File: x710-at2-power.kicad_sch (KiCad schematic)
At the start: 121 parts, among them U4 EZX710AT2_S_LMR5

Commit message: [#80813] Add OCuLink connector
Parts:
- renumbered C35 to C100, C36 to C101, C37 to C102, C38 to C103, C81 to C104, C82 to C105, C83 to C106, C84 to C107, C85 to C108, C86 to C109, C108 to C110, C13 to C111, C12 to C112, C11 to C113, C10 to C114, C109 to C115, C110 to C116, C118 to C117, C119 to C118, C117 to C119, C113 to C120, C114 to C121, C115 to C122, C116 to C123, C111 to C124, C112 to C125, C125 to C126, C126 to C127, C124 to C128, C120 to C129, C121 to C130, C122 to C131, C123 to C132, C135 to C133, C140 to C134, C136 to C135, C137 to C136, C138 to C137, C139 to C138, C141 to C139, C143 to C140, C142 to C141, C144 to C142, C145 to C143, C87 to C32, C88 to C33, C89 to C34, C90 to C35, C91 to C36, C92 to C37, C93 to C38, C94 to C39, C95 to C40, C74 to C41, C63 to C42, C64 to C43, C65 to C44, C66 to C45, C67 to C46, C68 to C47, C69 to C48, C70 to C49, C71 to C50, C72 to C51, C73 to C52, C146 to C53, C147 to C54, C148 to C55, C149 to C56, C150 to C57, C151 to C58, C40 to C59, C41 to C60, C42 to C61, C43 to C62, C44 to C63, C45 to C64, C46 to C65, C47 to C66, C48 to C67, C49 to C68, C50 to C69, C51 to C70, C52 to C71, C53 to C72, C54 to C73, C55 to C74, C56 to C75, C61 to C76, C62 to C77, C59 to C78, C60 to C79, C58 to C80, C57 to C81, C152 to C82, C153 to C83, C34 to C84, C75 to C85, C76 to C86, C77 to C87, C78 to C88, C79 to C89, C80 to C90, C39 to C91, C127 to C92, C132 to C93, C133 to C94, C128 to C95, C129 to C96, C130 to C97, C131 to C98, C134 to C99, FB7 to FB3, FB5 to FB4, FB2 to FB5, FB4 to FB6, FB6 to FB7, L6 to L3

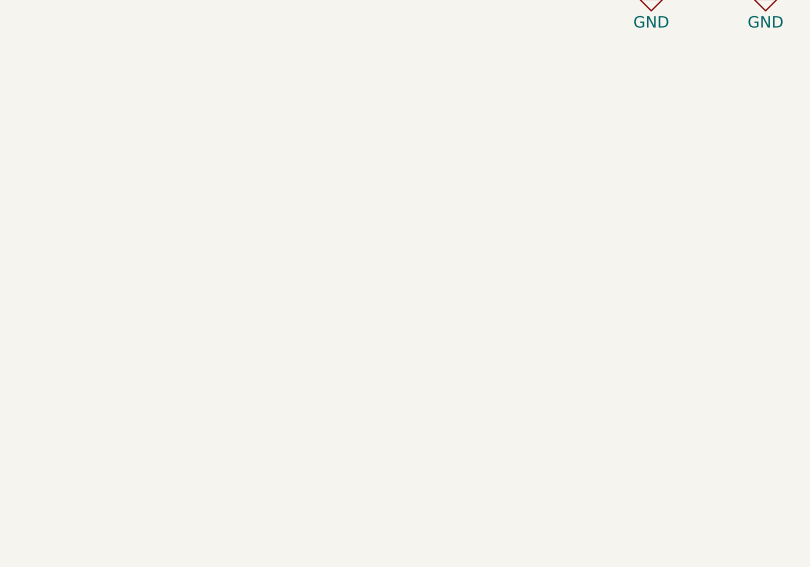
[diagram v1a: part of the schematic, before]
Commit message: [#80813] Add power input connectors, heatsink, mounting, draft component placement
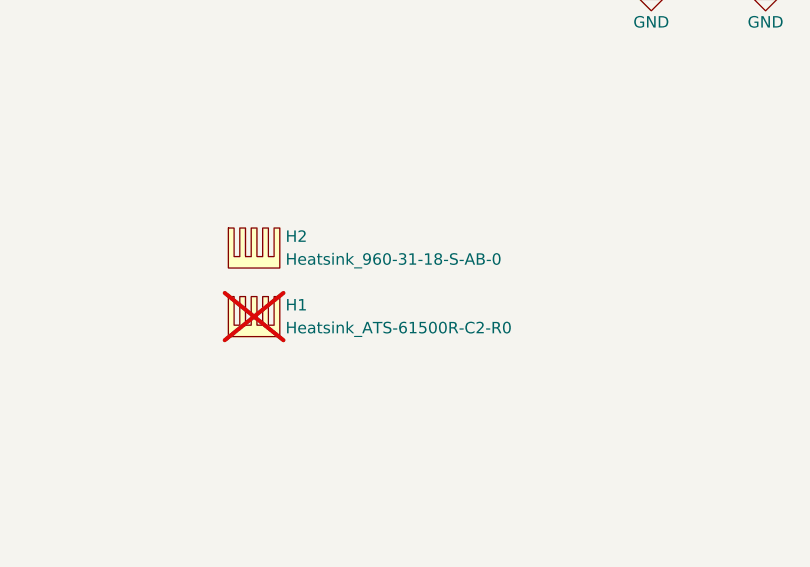
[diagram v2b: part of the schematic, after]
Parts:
- added H1: Heatsink_ATS-61500R-C2-R0, antmicro-footprints:Heatsink_ATS-61500R-C2-R0, symbol antmicroMechanicalParts:Heatsink_ATS-61500R-C2-R0
- added H2: Heatsink_960-31-18-S-AB-0, antmicro-footprints:Heatsink_960-31-18-S-AB-0, symbol antmicroMechanicalParts:Heatsink_960-31-18-S-AB-0
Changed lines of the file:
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@@
 	)
 	(symbol
+		(lib_id "antmicroMechanicalParts:Heatsink_960-31-18-S-AB-0")
+		(at 223.52 179.07 0)
+		(unit 1)
+		(exclude_from_sim no)
+		(in_bom yes)
+		(on_board yes)
+		(dnp no)
+		(fields_autoplaced yes)
+		(property "Reference" "H2"
+			(at 229.87 180.0225 0)
+			(effects
+				(font
+					(size 1.27 1.27)
+					(thickness 0.15)
+				)
+				(justify left)
+			)
+		)
+		(property "Value" "Heatsink_960-31-18-S-AB-0"
+			(at 229.87 182.5625 0)
+			(effects
+				(font
+					(size 1.27 1.27)
+					(thickness 0.15)
+				)
+				(justify left)
+			)
+		)
+		(property "Footprint" "antmicro-footprints:Heatsink_960-31-18-S-AB-0"
+			(at 241.3 186.69 0)
+			(effects
+				(font
+					(size 1.27 1.27)
+					(thickness 0.15)
+				)
+				(justify left bottom)
+				(hide yes)
+			)
+		)
+		(property "Datasheet" "https://media.digikey.com/pdf/Data%20Sheets/Wakefield%20Thermal%20PDFs/960_Series.pdf"
+			(at 241.3 189.23 0)
+			(effects
+				(font
+					(size 1.27 1.27)
+					(thickness 0.15)
+				)
+				(justify left bottom)
+				(hide yes)
+			)
+		)
+		(property "Description" "Heat Sink BGA Aluminum Top Mount"
+			(at 223.52 179.07 0)
+			(effects
+				(font
+					(size 1.27 1.27)
+				)
+				(hide yes)
+			)
+		)
+		(property "MPN" "960-31-18-S-AB-0"
+			(at 241.3 191.77 0)
+			(effects
+				(font
+					(size 1.27 1.27)
+					(thickness 0.15)
+				)
+				(justify left bottom)
+				(hide yes)
+			)
+		)
+		(property "Manufacturer" "Wakefield-Vette"
+			(at 241.3 194.31 0)
+			(effects
+				(font
+					(size 1.27 1.27)
+					(thickness 0.15)
+				)
+				(justify left bottom)
+				(hide yes)
+			)
+		)
+		(property "Author" "Antmicro"
+			(at 241.3 196.85 0)
+			(effects
+				(font
+					(size 1.27 1.27)
+					(thickness 0.15)
+				)
+				(justify left bottom)
+				(hide yes)
+			)
+		)
+		(property "License" "Apache-2.0"
+			(at 241.3 199.39 0)
+			(effects
+				(font
+					(size 1.27 1.27)
+					(thickness 0.15)
+				)
+				(justify left bottom)
+				(hide yes)
+			)
+		)
+		(instances
+			(project ""
+				(path "/04bda987-e5eb-48b4-9e90-d8211dc11b39/745fdd8b-25af-4553-a7ea-a0fa564ee0a7"
+					(reference "H2")
+					(unit 1)
+				)
+			)
+		)
+	)
+	(symbol
 		(lib_id "antmicropower:GND")
 		(at 361.95 76.2 0)
@@
 					(unit 1)
 				)
+			)
+		)
+	)
+	(symbol
+		(lib_id "antmicroMechanicalParts:Heatsink_ATS-61500R-C2-R0")
+		(at 223.52 186.69 0)
+		(unit 1)
+		(exclude_from_sim no)
+		(in_bom no)
+		(on_board yes)
+		(dnp yes)
+		(fields_autoplaced yes)
+		(property "Reference" "H1"
+			(at 229.87 187.6425 0)
+			(effects
+				(font
+					(size 1.27 1.27)
+					(thickness 0.15)
+				)
+				(justify left)
+			)
+		)
+		(property "Value" "Heatsink_ATS-61500R-C2-R0"
+			(at 229.87 190.1825 0)
+			(effects
+				(font
+					(size 1.27 1.27)
+					(thickness 0.15)
+				)
+				(justify left)
+			)
+		)
+		(property "Footprint" "antmicro-footprints:Heatsink_ATS-61500R-C2-R0"
+			(at 241.3 194.31 0)
+			(effects
+				(font
+					(size 1.27 1.27)
+					(thickness 0.15)
+				)
+				(justify left bottom)
+				(hide yes)
+			)
+		)
+		(property "Datasheet" "https://www.qats.com/DataSheet/ATS-61500-Series-C2-R0"
+			(at 241.3 196.85 0)
+			(effects
+				(font
+					(size 1.27 1.27)
+					(thickness 0.15)
+				)
+				(justify left bottom)
+				(hide yes)
+			)
+		)
+		(property "Description" "Heat Sinks fanSINK Assembly with Mounting Hardware"
+			(at 223.52 186.69 0)
+			(effects
+				(font
+					(size 1.27 1.27)
+				)
+				(hide yes)
+			)
+		)
+		(property "MPN" "ATS-61500R-C2-R0"
+			(at 241.3 199.39 0)
+			(effects
+				(font
+					(size 1.27 1.27)
+					(thickness 0.15)
+				)
+				(justify left bottom)
+				(hide yes)
+			)
+		)
+		(property "Manufacturer" "Advanced Thermal Solutions"
+			(at 241.3 201.93 0)
+			(effects
+				(font
+					(size 1.27 1.27)
+					(thickness 0.15)
+				)
+				(justify left bottom)
+				(hide yes)
+			)
+		)
+		(property "Author" "Antmicro"
+			(at 241.3 204.47 0)
+			(effects
+				(font
+					(size 1.27 1.27)
+					(thickness 0.15)
+				)
+				(justify left bottom)
+				(hide yes)
+			)
+		)
+		(property "License" "Apache-2.0"
+			(at 241.3 207.01 0)
+			(effects
+				(font
+					(size 1.27 1.27)
+					(thickness 0.15)
+				)
+				(justify left bottom)
+				(hide yes)
+			)
+		)
+		(instances
+			(project ""
+				(path "/04bda987-e5eb-48b4-9e90-d8211dc11b39/745fdd8b-25af-4553-a7ea-a0fa564ee0a7"
+					(reference "H1")
+					(unit 1)
+				)

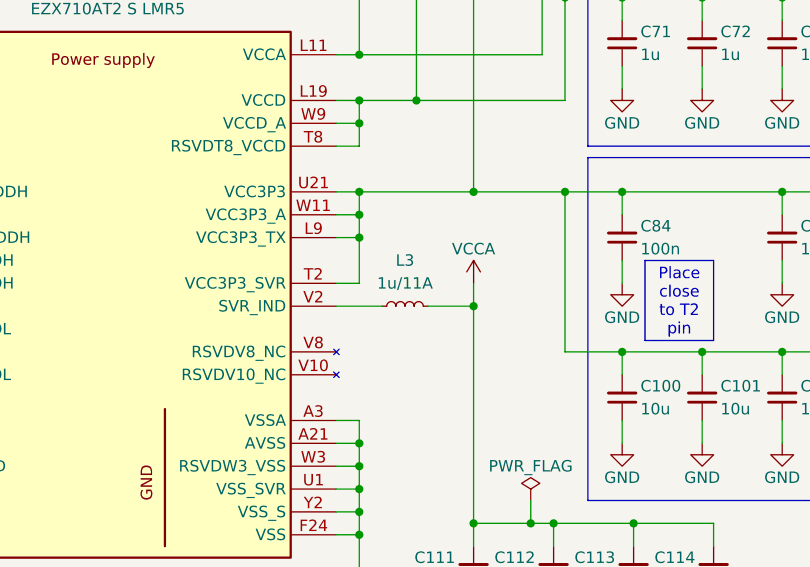
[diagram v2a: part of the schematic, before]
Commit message: [#80813] Change inductors, minor PCB changes
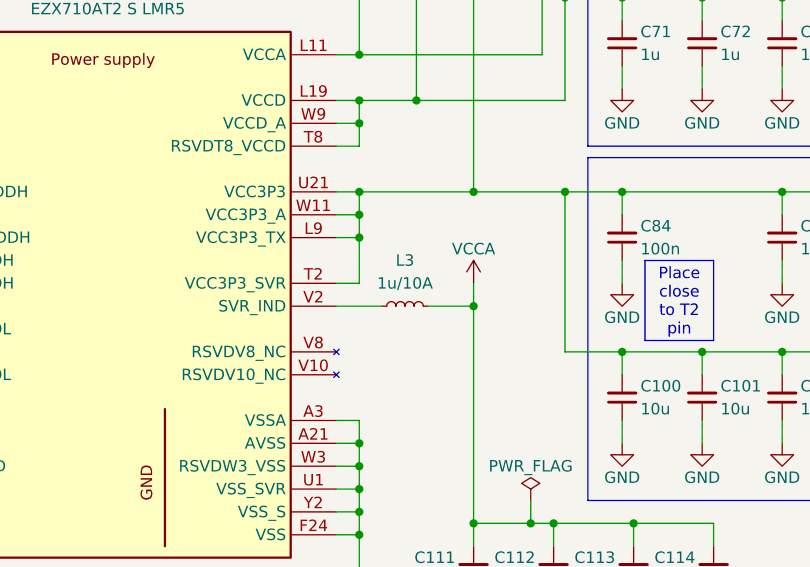
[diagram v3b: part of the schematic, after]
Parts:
- removed L3: L_1u_11A_Coilcraft-XFL4020, antmicro-footprints:L_Coilcraft-XFL4020, symbol antmicroFixedInductors:L_1u_11A_Coilcraft-XFL4020
- added L3: L_1u_10A_Bourns-SRP4021HMT, antmicro-footprints:L_Bourns-SRP4021HMT, symbol antmicroFixedInductors:L_1u_10A_Bourns-SRP4021HMT
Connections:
- net VCCA: now also L3.2
- net at U4.V2 (SVR_IND): now also L3.1
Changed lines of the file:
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@@
 	)
 	(symbol
+		(lib_id "antmicroFixedInductors:L_1u_10A_Bourns-SRP4021HMT")
+		(at 273.05 118.11 0)
+		(unit 1)
+		(exclude_from_sim no)
+		(in_bom yes)
+		(on_board yes)
+		(dnp no)
+		(fields_autoplaced yes)
+		(property "Reference" "L3"
+			(at 275.59 113.03 0)
+			(effects
+				(font
+					(size 1.27 1.27)
+					(thickness 0.15)
+				)
+			)
+		)
+		(property "Value" "L_1u_10A_Bourns-SRP4021HMT"
+			(at 288.29 128.27 0)
+			(effects
+				(font
+					(size 1.27 1.27)
+					(thickness 0.15)
+				)
+				(justify left bottom)
+				(hide yes)
+			)
+		)
+		(property "Footprint" "antmicro-footprints:L_Bourns-SRP4021HMT"
+			(at 288.29 130.81 0)
+			(effects
+				(font
+					(size 1.27 1.27)
+					(thickness 0.15)
+				)
+				(justify left bottom)
+				(hide yes)
+			)
+		)
+		(property "Datasheet" "https://www.mouser.pl/datasheet/2/54/Bourns_04_01_2025_SRP4021HMT_Datasheet-3580094.pdf"
+			(at 288.29 133.35 0)
+			(effects
+				(font
+					(size 1.27 1.27)
+					(thickness 0.15)
+				)
+				(justify left bottom)
+				(hide yes)
+			)
+		)
+		(property "Description" "Power Inductors - SMD Ind,4.1x4.2x1.9mm,1uH+/-20%,10A, Shielded"
+			(at 288.29 135.89 0)
+			(effects
+				(font
+					(size 1.27 1.27)
+					(thickness 0.15)
+				)
+				(justify left bottom)
+				(hide yes)
+			)
+		)
+		(property "Val" "1u/10A"
+			(at 275.59 115.57 0)
+			(effects
+				(font
+					(size 1.27 1.27)
+					(thickness 0.15)
+				)
+			)
+		)
+		(property "Manufacturer" "Bourns"
+			(at 288.29 138.43 0)
+			(effects
+				(font
+					(size 1.27 1.27)
+					(thickness 0.15)
+				)
+				(justify left bottom)
+				(hide yes)
+			)
+		)
+		(property "MPN" "SRP4021HMT-1R0M"
+			(at 288.29 140.97 0)
+			(effects
+				(font
+					(size 1.27 1.27)
+					(thickness 0.15)
+				)
+				(justify left bottom)
+				(hide yes)
+			)
+		)
+		(property "ISat" ""
+			(at 287.02 134.62 0)
+			(effects
+				(font
+					(size 1.27 1.27)
+				)
+				(justify left)
+				(hide yes)
+			)
+		)
+		(property "Isat" "8A"
+			(at 288.29 143.51 0)
+			(effects
+				(font
+					(size 1.27 1.27)
+					(thickness 0.15)
+				)
+				(justify left bottom)
+				(hide yes)
+			)
+		)
+		(property "IMax" ""
+			(at 287.02 138.43 0)
+			(effects
+				(font
+					(size 1.27 1.27)
+					(thickness 0.15)
+				)
+				(justify left bottom)
+				(hide yes)
+			)
+		)
+		(property "Imax" "10A"
+			(at 288.29 146.05 0)
+			(effects
+				(font
+					(size 1.27 1.27)
+					(thickness 0.15)
+				)
+				(justify left bottom)
+				(hide yes)
+			)
+		)
+		(property "Size" "4.2x4.1"
+			(at 288.29 148.59 0)
+			(effects
+				(font
+					(size 1.27 1.27)
+					(thickness 0.15)
+				)
+				(justify left bottom)
+				(hide yes)
+			)
+		)
+		(property "Author" "Antmicro"
+			(at 288.29 151.13 0)
+			(effects
+				(font
+					(size 1.27 1.27)
+					(thickness 0.15)
+				)
+				(justify left bottom)
+				(hide yes)
+			)
+		)
+		(property "License" "Apache-2.0"
+			(at 288.29 153.67 0)
+			(effects
+				(font
+					(size 1.27 1.27)
+					(thickness 0.15)
+				)
+				(justify left bottom)
+				(hide yes)
+			)
+		)
+		(pin "1"
+		)
+		(pin "2"
+		)
+		(instances
+			(project "10-gbe-expansion"
+				(path "/04bda987-e5eb-48b4-9e90-d8211dc11b39/745fdd8b-25af-4553-a7ea-a0fa564ee0a7"
+					(reference "L3")
+					(unit 1)
+				)
+			)
+		)
+	)
+	(symbol
 		(lib_id "antmicroFerriteBeadsandChips:FB_33Z_3A_Murata-BLM18PG_0603")
 		(at 45.72 172.72 0)
@@
 					(unit 1)
 				)
-			)
-		)
-	)
-	(symbol
-		(lib_id "antmicroFixedInductors:L_1u_11A_Coilcraft-XFL4020")
-		(at 273.05 118.11 0)
-		(unit 1)
-		(exclude_from_sim no)
-		(in_bom yes)
-		(on_board yes)
-		(dnp no)
-		(fields_autoplaced yes)
-		(property "Reference" "L3"
-			(at 275.59 113.03 0)
-			(effects
-				(font
-					(size 1.27 1.27)
-					(thickness 0.15)
-				)
-			)
-		)
-		(property "Value" "L_1u_11A_Coilcraft-XFL4020"
-			(at 287.02 120.65 0)
-			(effects
-				(font
-					(size 1.27 1.27)
-					(thickness 0.15)
-				)
-				(justify left bottom)
-				(hide yes)
-			)
-		)
-		(property "Footprint" "antmicro-footprints:L_Coilcraft-XFL4020"
-			(at 287.02 125.73 0)
-			(effects
-				(font
-					(size 1.27 1.27)
-					(thickness 0.15)
-				)
-				(justify left bottom)
-				(hide yes)
-			)
-		)
-		(property "Datasheet" "https://www.coilcraft.com/getmedia/50632d43-da1b-4cdb-8ab4-3029cab51df3/xfl4020.pdf"
-			(at 287.02 128.27 0)
-			(effects
-				(font
-					(size 1.27 1.27)
-					(thickness 0.15)
-				)
-				(justify left bottom)
-				(hide yes)
-			)
-		)
-		(property "Description" "Power Inductor (SMD), 1 µH, 11 A, Shielded, 4.5 A, XFL4020"
-			(at 273.05 118.11 0)
-			(effects
-				(font
-					(size 1.27 1.27)
-				)
-				(hide yes)
-			)
-		)
-		(property "Val" "1u/11A"
-			(at 275.59 115.57 0)
-			(effects
-				(font
-					(size 1.27 1.27)
-					(thickness 0.15)
-				)
-			)
-		)
-		(property "Manufacturer" "Coilcraft"
-			(at 287.02 130.81 0)
-			(effects
-				(font
-					(size 1.27 1.27)
-					(thickness 0.15)
-				)
-				(justify left bottom)
-				(hide yes)
-			)
-		)
-		(property "MPN" "XFL4020-102MEC"
-			(at 287.02 133.35 0)
-			(effects
-				(font
-					(size 1.27 1.27)
-					(thickness 0.15)
-				)
-				(justify left bottom)
-				(hide yes)
-			)
-		)
-		(property "ISat" "5.4 A"
-			(at 287.02 134.62 0)
-			(effects
-				(font
-					(size 1.27 1.27)
-				)
-				(justify left)
-				(hide yes)
-			)
-		)
-		(property "IMax" "11 A"
-			(at 287.02 138.43 0)
-			(effects
-				(font
-					(size 1.27 1.27)
-					(thickness 0.15)
-				)
-				(justify left bottom)
-				(hide yes)
-			)
-		)
-		(property "Size" "4.3x4.3"
-			(at 287.02 140.97 0)
-			(effects
-				(font
-					(size 1.27 1.27)
-					(thickness 0.15)
-				)
-				(justify left bottom)
-				(hide yes)
-			)
-		)
-		(property "Author" "Antmicro"
-			(at 287.02 143.51 0)
-			(effects
-				(font
-					(size 1.27 1.27)
-					(thickness 0.15)
-				)
-				(justify left bottom)
-				(hide yes)
-			)
-		)
-		(property "License" "Apache-2.0"
-			(at 287.02 146.05 0)
-			(effects
-				(font
-					(size 1.27 1.27)
-					(thickness 0.15)
-				)
-				(justify left bottom)
-				(hide yes)
-			)
-		)
-		(pin "1"
-		)
-		(pin "2"
-		)
-		(instances
-			(project ""
-				(path "/04bda987-e5eb-48b4-9e90-d8211dc11b39/745fdd8b-25af-4553-a7ea-a0fa564ee0a7"
-					(reference "L3")
-					(unit 1)
-				)

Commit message: [#81595] Update symbols from library
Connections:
- no-connect marks 0 -> 2
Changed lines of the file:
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@@
 		(color 0 0 0 0)
 	)
+	(no_connect
+		(at 267.97 125.73)
+	)
+	(no_connect
+		(at 267.97 123.19)
+	)
 	(wire
 		(pts
@@
 			)
 		)
-		(property "Datasheet" "https://www.mouser.pl/datasheet/2/54/Bourns_04_01_2025_SRP4021HMT_Datasheet-3580094.pdf"
+		(property "Datasheet" "https://www.mouser.com/datasheet/2/54/Bourns_04_01_2025_SRP4021HMT_Datasheet-3580094.pdf"
 			(at 288.29 133.35 0)
 			(effects
@@
 		(pin "M22"
 		)
-		(pin "M31"
+		(pin "V34"
 		)
 		(pin "G27"
@@
 		(pin "J39"
 		)
-		(pin "M15"
-		)
 		(pin "D42"

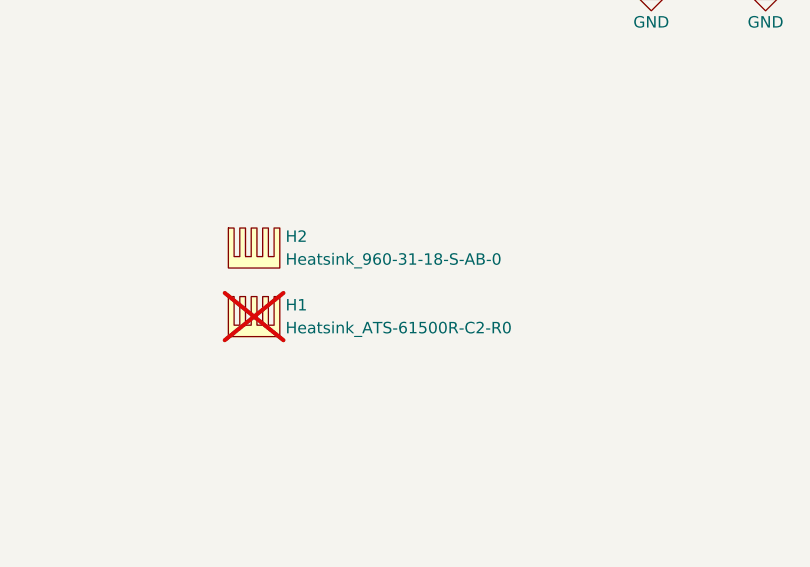
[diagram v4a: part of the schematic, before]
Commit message: [#85196] Update PCB from schematic, remove second heat sink
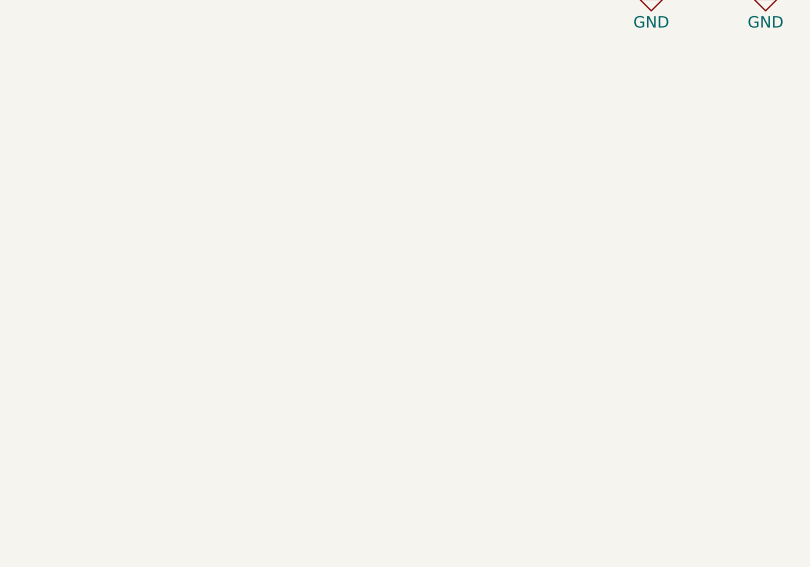
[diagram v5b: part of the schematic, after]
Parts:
- removed H1: Heatsink_ATS-61500R-C2-R0, antmicro-footprints:Heatsink_ATS-61500R-C2-R0, symbol antmicroMechanicalParts:Heatsink_ATS-61500R-C2-R0
- removed H2: Heatsink_960-31-18-S-AB-0, antmicro-footprints:Heatsink_960-31-18-S-AB-0, symbol antmicroMechanicalParts:Heatsink_960-31-18-S-AB-0
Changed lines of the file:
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@@
 	)
 	(symbol
-		(lib_id "antmicroMechanicalParts:Heatsink_960-31-18-S-AB-0")
-		(at 223.52 179.07 0)
-		(unit 1)
-		(exclude_from_sim no)
-		(in_bom yes)
-		(on_board yes)
-		(dnp no)
-		(fields_autoplaced yes)
-		(property "Reference" "H2"
-			(at 229.87 180.0225 0)
-			(effects
-				(font
-					(size 1.27 1.27)
-					(thickness 0.15)
-				)
-				(justify left)
-			)
-		)
-		(property "Value" "Heatsink_960-31-18-S-AB-0"
-			(at 229.87 182.5625 0)
-			(effects
-				(font
-					(size 1.27 1.27)
-					(thickness 0.15)
-				)
-				(justify left)
-			)
-		)
-		(property "Footprint" "antmicro-footprints:Heatsink_960-31-18-S-AB-0"
-			(at 241.3 186.69 0)
-			(effects
-				(font
-					(size 1.27 1.27)
-					(thickness 0.15)
-				)
-				(justify left bottom)
-				(hide yes)
-			)
-		)
-		(property "Datasheet" "https://media.digikey.com/pdf/Data%20Sheets/Wakefield%20Thermal%20PDFs/960_Series.pdf"
-			(at 241.3 189.23 0)
-			(effects
-				(font
-					(size 1.27 1.27)
-					(thickness 0.15)
-				)
-				(justify left bottom)
-				(hide yes)
-			)
-		)
-		(property "Description" "Heat Sink BGA Aluminum Top Mount"
-			(at 223.52 179.07 0)
-			(effects
-				(font
-					(size 1.27 1.27)
-				)
-				(hide yes)
-			)
-		)
-		(property "MPN" "960-31-18-S-AB-0"
-			(at 241.3 191.77 0)
-			(effects
-				(font
-					(size 1.27 1.27)
-					(thickness 0.15)
-				)
-				(justify left bottom)
-				(hide yes)
-			)
-		)
-		(property "Manufacturer" "Wakefield-Vette"
-			(at 241.3 194.31 0)
-			(effects
-				(font
-					(size 1.27 1.27)
-					(thickness 0.15)
-				)
-				(justify left bottom)
-				(hide yes)
-			)
-		)
-		(property "Author" "Antmicro"
-			(at 241.3 196.85 0)
-			(effects
-				(font
-					(size 1.27 1.27)
-					(thickness 0.15)
-				)
-				(justify left bottom)
-				(hide yes)
-			)
-		)
-		(property "License" "Apache-2.0"
-			(at 241.3 199.39 0)
-			(effects
-				(font
-					(size 1.27 1.27)
-					(thickness 0.15)
-				)
-				(justify left bottom)
-				(hide yes)
-			)
-		)
-		(instances
-			(project ""
-				(path "/04bda987-e5eb-48b4-9e90-d8211dc11b39/745fdd8b-25af-4553-a7ea-a0fa564ee0a7"
-					(reference "H2")
-					(unit 1)
-				)
-			)
-		)
-	)
-	(symbol
 		(lib_id "antmicropower:GND")
 		(at 361.95 76.2 0)
@@
 					(unit 1)
 				)
-			)
-		)
-	)
-	(symbol
-		(lib_id "antmicroMechanicalParts:Heatsink_ATS-61500R-C2-R0")
-		(at 223.52 186.69 0)
-		(unit 1)
-		(exclude_from_sim no)
-		(in_bom no)
-		(on_board yes)
-		(dnp yes)
-		(fields_autoplaced yes)
-		(property "Reference" "H1"
-			(at 229.87 187.6425 0)
-			(effects
-				(font
-					(size 1.27 1.27)
-					(thickness 0.15)
-				)
-				(justify left)
-			)
-		)
-		(property "Value" "Heatsink_ATS-61500R-C2-R0"
-			(at 229.87 190.1825 0)
-			(effects
-				(font
-					(size 1.27 1.27)
-					(thickness 0.15)
-				)
-				(justify left)
-			)
-		)
-		(property "Footprint" "antmicro-footprints:Heatsink_ATS-61500R-C2-R0"
-			(at 241.3 194.31 0)
-			(effects
-				(font
-					(size 1.27 1.27)
-					(thickness 0.15)
-				)
-				(justify left bottom)
-				(hide yes)
-			)
-		)
-		(property "Datasheet" "https://www.qats.com/DataSheet/ATS-61500-Series-C2-R0"
-			(at 241.3 196.85 0)
-			(effects
-				(font
-					(size 1.27 1.27)
-					(thickness 0.15)
-				)
-				(justify left bottom)
-				(hide yes)
-			)
-		)
-		(property "Description" "Heat Sinks fanSINK Assembly with Mounting Hardware"
-			(at 223.52 186.69 0)
-			(effects
-				(font
-					(size 1.27 1.27)
-				)
-				(hide yes)
-			)
-		)
-		(property "MPN" "ATS-61500R-C2-R0"
-			(at 241.3 199.39 0)
-			(effects
-				(font
-					(size 1.27 1.27)
-					(thickness 0.15)
-				)
-				(justify left bottom)
-				(hide yes)
-			)
-		)
-		(property "Manufacturer" "Advanced Thermal Solutions"
-			(at 241.3 201.93 0)
-			(effects
-				(font
-					(size 1.27 1.27)
-					(thickness 0.15)
-				)
-				(justify left bottom)
-				(hide yes)
-			)
-		)
-		(property "Author" "Antmicro"
-			(at 241.3 204.47 0)
-			(effects
-				(font
-					(size 1.27 1.27)
-					(thickness 0.15)
-				)
-				(justify left bottom)
-				(hide yes)
-			)
-		)
-		(property "License" "Apache-2.0"
-			(at 241.3 207.01 0)
-			(effects
-				(font
-					(size 1.27 1.27)
-					(thickness 0.15)
-				)
-				(justify left bottom)
-				(hide yes)
-			)
-		)
-		(instances
-			(project ""
-				(path "/04bda987-e5eb-48b4-9e90-d8211dc11b39/745fdd8b-25af-4553-a7ea-a0fa564ee0a7"
-					(reference "H1")
-					(unit 1)
-				)
